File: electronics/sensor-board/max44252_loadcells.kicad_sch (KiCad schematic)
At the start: 21 parts

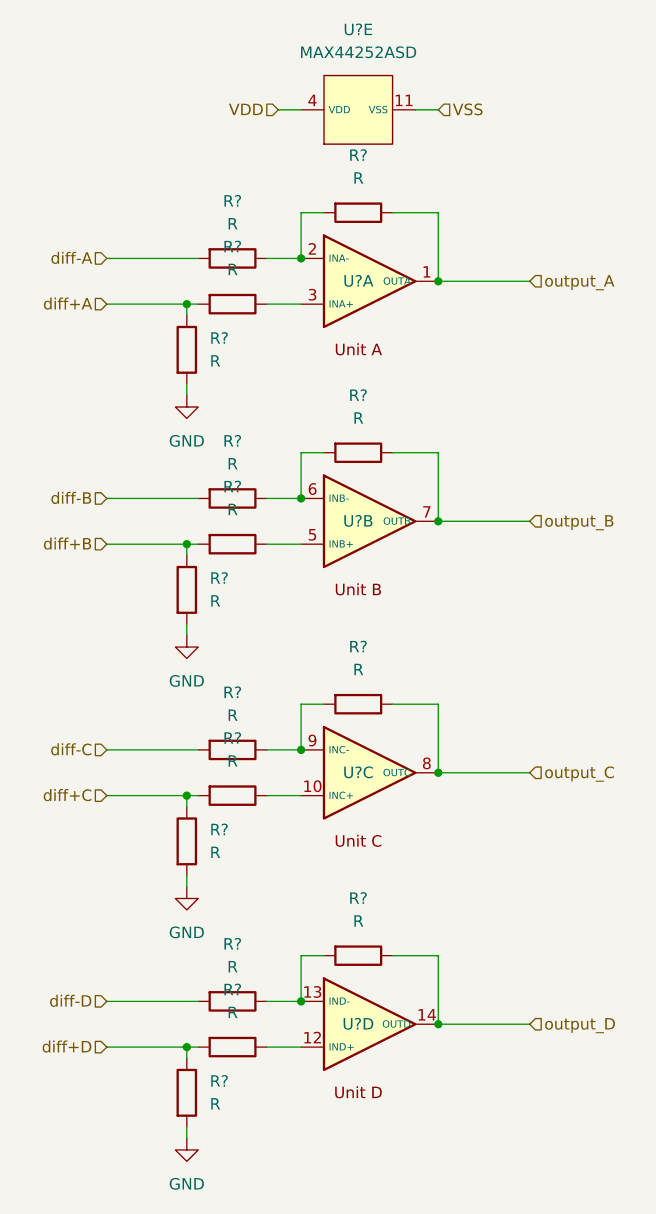
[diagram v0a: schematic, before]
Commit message: work on sensor-board
added MCP960 footprint
finished MCP960 array schematic
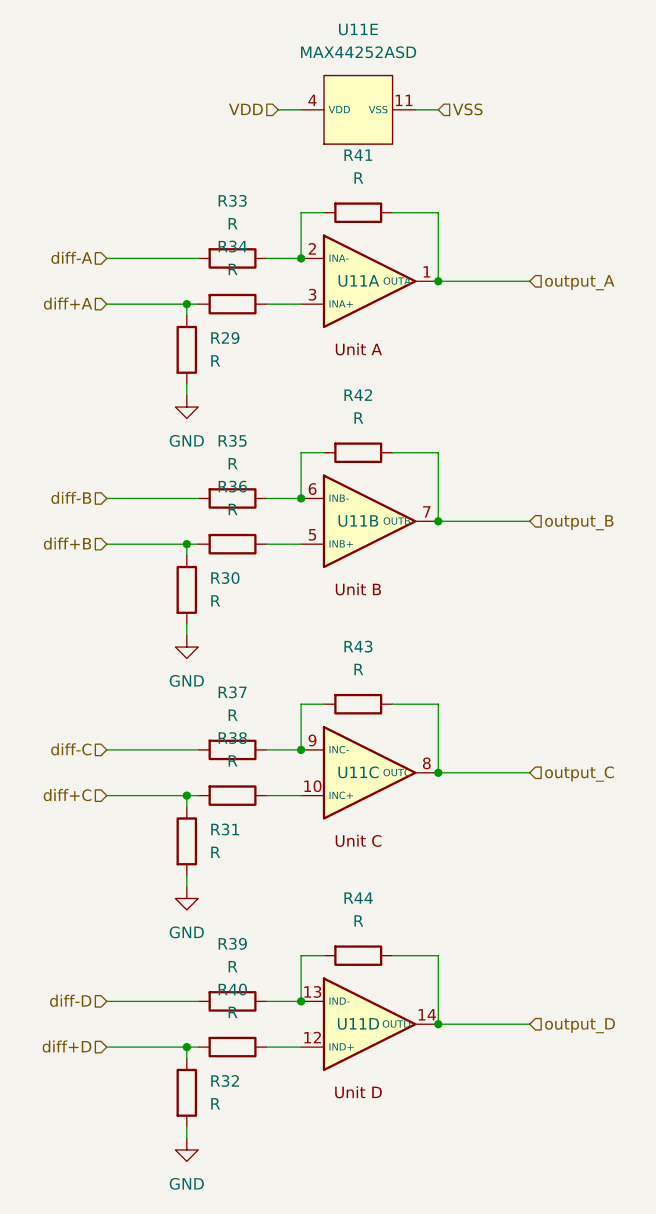
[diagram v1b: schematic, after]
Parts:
- removed R? (x16): R, symbol Device:R
- removed U? (x5): MAX44252ASD, symbol MAX44252ASD_Custom:MAX44252ASD
- added R29, R30, R31, R32, R33, R34, R35, R36, R37, R38, R39, R40, R41, R42, R43, R44: R, Resistor_SMD:R_0603_1608Metric, symbol Device:R
- added U11: MAX44252ASD, MAX44252ASD-:MAX44252ASD&plus_, symbol MAX44252ASD_Custom:MAX44252ASD
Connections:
- net GND: now also R29.2, R30.2, R31.2, R32.2
- net VDD: now also U11.4 (VDD)
- net VSS: now also U11.11 (VSS)
- net diff+A: now also R29.1, R34.2
- net diff+B: now also R30.1, R36.2
- net diff+C: now also R31.1, R38.2
- net diff+D: now also R32.1, R40.2
- net diff-A: now also R33.2
- net diff-B: now also R35.2
- net diff-C: now also R37.2
- net diff-D: now also R39.2
- net output_A: now also R41.1, U11.1 (OUTA)
- net output_B: now also R42.1, U11.7 (OUTB)
- net output_C: now also R43.1, U11.8 (OUTC)
- net output_D: now also R44.1, U11.14 (OUTD)
- new net: R40.1, U11.12 (IND+)
- new net: R34.1, U11.3 (INA+)
- new net: R38.1, U11.10 (INC+)
- new net: R39.1, R44.2, U11.13 (IND-)
- new net: R33.1, R41.2, U11.2 (INA-)
- new net: R37.1, R43.2, U11.9 (INC-)
- new net: R35.1, R42.2, U11.6 (INB-)
- new net: R36.1, U11.5 (INB+)

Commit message: work on sensor-board
finishing sub-circuits
switching mcu to stm32f105
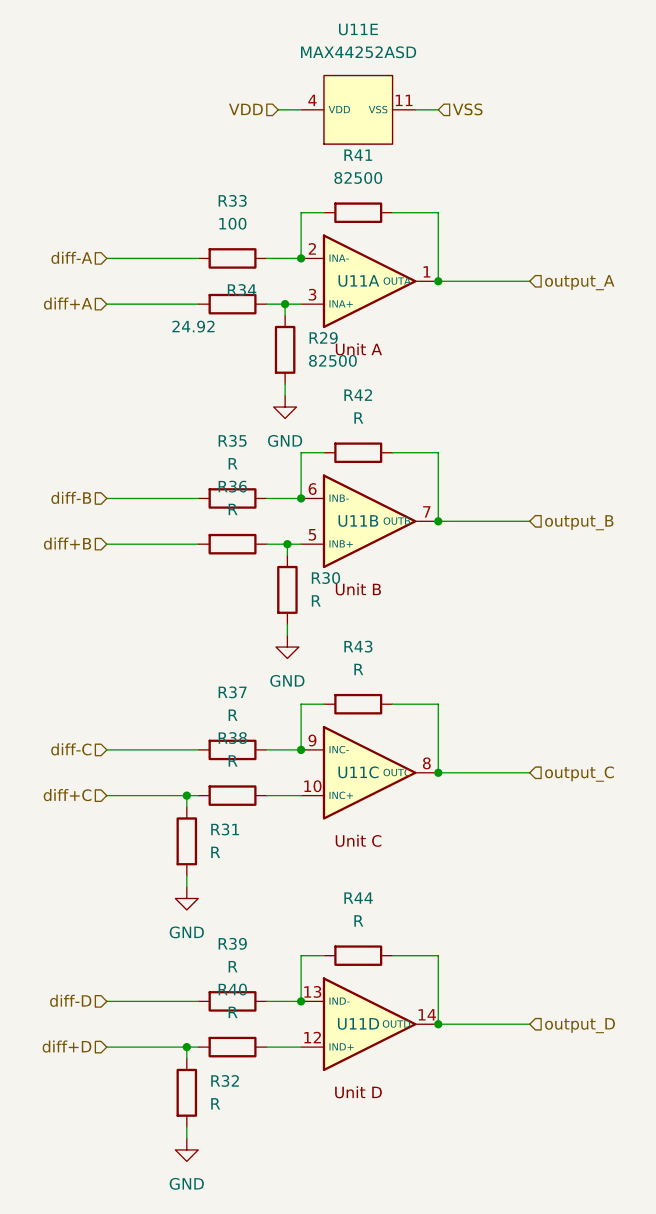
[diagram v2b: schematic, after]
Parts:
- R29, R41: value R -> 82500
- R33: value R -> 100
- R34: value R -> 24.92; note: (none) -> add series res for adjustment
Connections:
- net diff+A: no longer R29.1
- net diff+B: no longer R30.1
- net at R34.1, U11.3 (INA+): now also R29.1
- net at R36.1, U11.5 (INB+): now also R30.1
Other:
- moved on the sheet: R29, R30
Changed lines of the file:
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@@
 (kicad_sch (version 20210621) (generator eeschema)
   (paper "A4")
-  (junction (at 134.62 66.04) (diameter 0) (color 0 0 0 0))
-  (junction (at 134.62 92.71) (diameter 0) (color 0 0 0 0))
   (junction (at 134.62 120.65) (diameter 0) (color 0 0 0 0))
   (junction (at 134.62 148.59) (diameter 0) (color 0 0 0 0))
+  (junction (at 145.542 66.04) (diameter 0) (color 0 0 0 0))
+  (junction (at 145.796 92.71) (diameter 0) (color 0 0 0 0))
   (junction (at 147.32 60.96) (diameter 0) (color 0 0 0 0))
   (junction (at 147.32 87.63) (diameter 0) (color 0 0 0 0))
@@
     (stroke (width 0) (type default) (color 0 0 0 0))
   )
-  (wire (pts (xy 125.73 66.04) (xy 134.62 66.04))
+  (wire (pts (xy 125.73 66.04) (xy 135.89 66.04))
     (stroke (width 0) (type default) (color 0 0 0 0))
   )
@@
     (stroke (width 0) (type default) (color 0 0 0 0))
   )
-  (wire (pts (xy 125.73 92.71) (xy 134.62 92.71))
+  (wire (pts (xy 125.73 92.71) (xy 135.89 92.71))
     (stroke (width 0) (type default) (color 0 0 0 0))
   )
@@
     (stroke (width 0) (type default) (color 0 0 0 0))
   )
-  (wire (pts (xy 134.62 66.04) (xy 134.62 67.31))
-    (stroke (width 0) (type default) (color 0 0 0 0))
-  )
-  (wire (pts (xy 134.62 66.04) (xy 135.89 66.04))
-    (stroke (width 0) (type default) (color 0 0 0 0))
-  )
-  (wire (pts (xy 134.62 74.93) (xy 134.62 76.2))
-    (stroke (width 0) (type default) (color 0 0 0 0))
-  )
-  (wire (pts (xy 134.62 92.71) (xy 134.62 93.98))
-    (stroke (width 0) (type default) (color 0 0 0 0))
-  )
-  (wire (pts (xy 134.62 92.71) (xy 135.89 92.71))
-    (stroke (width 0) (type default) (color 0 0 0 0))
-  )
-  (wire (pts (xy 134.62 101.6) (xy 134.62 102.87))
-    (stroke (width 0) (type default) (color 0 0 0 0))
-  )
   (wire (pts (xy 134.62 120.65) (xy 134.62 121.92))
     (stroke (width 0) (type default) (color 0 0 0 0))
@@
     (stroke (width 0) (type default) (color 0 0 0 0))
   )
-  (wire (pts (xy 143.51 66.04) (xy 147.32 66.04))
+  (wire (pts (xy 143.51 66.04) (xy 145.542 66.04))
     (stroke (width 0) (type default) (color 0 0 0 0))
   )
@@
     (stroke (width 0) (type default) (color 0 0 0 0))
   )
-  (wire (pts (xy 143.51 92.71) (xy 147.32 92.71))
+  (wire (pts (xy 143.51 92.71) (xy 145.796 92.71))
     (stroke (width 0) (type default) (color 0 0 0 0))
   )
@@
   )
   (wire (pts (xy 144.78 44.45) (xy 147.32 44.45))
+    (stroke (width 0) (type default) (color 0 0 0 0))
+  )
+  (wire (pts (xy 145.542 66.04) (xy 145.542 67.31))
+    (stroke (width 0) (type default) (color 0 0 0 0))
+  )
+  (wire (pts (xy 145.542 66.04) (xy 147.32 66.04))
+    (stroke (width 0) (type default) (color 0 0 0 0))
+  )
+  (wire (pts (xy 145.542 74.93) (xy 145.542 76.2))
+    (stroke (width 0) (type default) (color 0 0 0 0))
+  )
+  (wire (pts (xy 145.796 92.71) (xy 145.796 93.98))
+    (stroke (width 0) (type default) (color 0 0 0 0))
+  )
+  (wire (pts (xy 145.796 92.71) (xy 147.32 92.71))
+    (stroke (width 0) (type default) (color 0 0 0 0))
+  )
+  (wire (pts (xy 145.796 101.6) (xy 145.796 102.87))
     (stroke (width 0) (type default) (color 0 0 0 0))
   )
@@
     (effects (font (size 1.27 1.27)) (justify left))
   )
-  (symbol (lib_id "power:GND") (at 134.62 76.2 0) (unit 1)
-    (in_bom yes) (on_board yes) (fields_autoplaced)
-    (property "Reference" "#PWR0175" (id 0) (at 134.62 82.55 0)
-      (effects (font (size 1.27 1.27)) hide)
-    )
-    (property "Value" "GND" (id 1) (at 134.62 81.28 0))
-    (property "Footprint" "" (id 2) (at 134.62 76.2 0)
-      (effects (font (size 1.27 1.27)) hide)
-    )
-    (property "Datasheet" "" (id 3) (at 134.62 76.2 0)
-      (effects (font (size 1.27 1.27)) hide)
-    )
-    (pin "1")
-  )
-  (symbol (lib_id "power:GND") (at 134.62 102.87 0) (unit 1)
-    (in_bom yes) (on_board yes) (fields_autoplaced)
-    (property "Reference" "#PWR0176" (id 0) (at 134.62 109.22 0)
-      (effects (font (size 1.27 1.27)) hide)
-    )
-    (property "Value" "GND" (id 1) (at 134.62 107.95 0))
-    (property "Footprint" "" (id 2) (at 134.62 102.87 0)
-      (effects (font (size 1.27 1.27)) hide)
-    )
-    (property "Datasheet" "" (id 3) (at 134.62 102.87 0)
-      (effects (font (size 1.27 1.27)) hide)
-    )
-    (pin "1")
-  )
   (symbol (lib_id "power:GND") (at 134.62 130.81 0) (unit 1)
     (in_bom yes) (on_board yes) (fields_autoplaced)
@@
     (pin "1")
   )
-  (symbol (lib_id "Device:R") (at 134.62 71.12 0) (unit 1)
-    (in_bom yes) (on_board yes) (fields_autoplaced)
-    (property "Reference" "R29" (id 0) (at 137.16 69.8499 0)
-      (effects (font (size 1.27 1.27)) (justify left))
-    )
-    (property "Value" "R" (id 1) (at 137.16 72.3899 0)
-      (effects (font (size 1.27 1.27)) (justify left))
-    )
-    (property "Footprint" "Resistor_SMD:R_0603_1608Metric" (id 2) (at 132.842 71.12 90)
-      (effects (font (size 1.27 1.27)) hide)
-    )
-    (property "Datasheet" "~" (id 3) (at 134.62 71.12 0)
-      (effects (font (size 1.27 1.27)) hide)
-    )
-    (pin "1")
-    (pin "2")
-  )
-  (symbol (lib_id "Device:R") (at 134.62 97.79 0) (unit 1)
-    (in_bom yes) (on_board yes) (fields_autoplaced)
-    (property "Reference" "R30" (id 0) (at 137.16 96.5199 0)
-      (effects (font (size 1.27 1.27)) (justify left))
-    )
-    (property "Value" "R" (id 1) (at 137.16 99.0599 0)
-      (effects (font (size 1.27 1.27)) (justify left))
-    )
-    (property "Footprint" "Resistor_SMD:R_0603_1608Metric" (id 2) (at 132.842 97.79 90)
-      (effects (font (size 1.27 1.27)) hide)
-    )
-    (property "Datasheet" "~" (id 3) (at 134.62 97.79 0)
-      (effects (font (size 1.27 1.27)) hide)
-    )
-    (pin "1")
-    (pin "2")
+  (symbol (lib_id "power:GND") (at 145.542 76.2 0) (unit 1)
+    (in_bom yes) (on_board yes) (fields_autoplaced)
+    (property "Reference" "#PWR0175" (id 0) (at 145.542 82.55 0)
+      (effects (font (size 1.27 1.27)) hide)
+    )
+    (property "Value" "GND" (id 1) (at 145.542 81.28 0))
+    (property "Footprint" "" (id 2) (at 145.542 76.2 0)
+      (effects (font (size 1.27 1.27)) hide)
+    )
+    (property "Datasheet" "" (id 3) (at 145.542 76.2 0)
+      (effects (font (size 1.27 1.27)) hide)
+    )
+    (pin "1")
+  )
+  (symbol (lib_id "power:GND") (at 145.796 102.87 0) (unit 1)
+    (in_bom yes) (on_board yes) (fields_autoplaced)
+    (property "Reference" "#PWR0176" (id 0) (at 145.796 109.22 0)
+      (effects (font (size 1.27 1.27)) hide)
+    )
+    (property "Value" "GND" (id 1) (at 145.796 107.95 0))
+    (property "Footprint" "" (id 2) (at 145.796 102.87 0)
+      (effects (font (size 1.27 1.27)) hide)
+    )
+    (property "Datasheet" "" (id 3) (at 145.796 102.87 0)
+      (effects (font (size 1.27 1.27)) hide)
+    )
+    (pin "1")
   )
   (symbol (lib_id "Device:R") (at 134.62 125.73 0) (unit 1)
@@
     (in_bom yes) (on_board yes) (fields_autoplaced)
     (property "Reference" "R33" (id 0) (at 139.7 54.61 90))
-    (property "Value" "R" (id 1) (at 139.7 57.15 90))
+    (property "Value" "100" (id 1) (at 139.7 57.15 90))
     (property "Footprint" "Resistor_SMD:R_0603_1608Metric" (id 2) (at 139.7 59.182 90)
       (effects (font (size 1.27 1.27)) hide)
@@
   )
   (symbol (lib_id "Device:R") (at 139.7 66.04 270) (unit 1)
-    (in_bom yes) (on_board yes) (fields_autoplaced)
-    (property "Reference" "R34" (id 0) (at 139.7 59.69 90))
-    (property "Value" "R" (id 1) (at 139.7 62.23 90))
+    (in_bom yes) (on_board yes)
+    (property "Reference" "R34" (id 0) (at 140.716 64.516 90))
+    (property "Value" "24.92" (id 1) (at 135.382 68.58 90))
     (property "Footprint" "Resistor_SMD:R_0603_1608Metric" (id 2) (at 139.7 64.262 90)
       (effects (font (size 1.27 1.27)) hide)
     )
     (property "Datasheet" "~" (id 3) (at 139.7 66.04 0)
+      (effects (font (size 1.27 1.27)) hide)
+    )
+    (property "note:" "add series res for adjustment" (id 4) (at 139.7 66.04 90)
       (effects (font (size 1.27 1.27)) hide)
     )
@@
     (pin "2")
   )
+  (symbol (lib_id "Device:R") (at 145.542 71.12 0) (unit 1)
+    (in_bom yes) (on_board yes) (fields_autoplaced)
+    (property "Reference" "R29" (id 0) (at 148.082 69.8499 0)
+      (effects (font (size 1.27 1.27)) (justify left))
+    )
+    (property "Value" "82500" (id 1) (at 148.082 72.3899 0)
+      (effects (font (size 1.27 1.27)) (justify left))
+    )
+    (property "Footprint" "Resistor_SMD:R_0603_1608Metric" (id 2) (at 143.764 71.12 90)
+      (effects (font (size 1.27 1.27)) hide)
+    )
+    (property "Datasheet" "~" (id 3) (at 145.542 71.12 0)
+      (effects (font (size 1.27 1.27)) hide)
+    )
+    (pin "1")
+    (pin "2")
+  )
+  (symbol (lib_id "Device:R") (at 145.796 97.79 0) (unit 1)
+    (in_bom yes) (on_board yes) (fields_autoplaced)
+    (property "Reference" "R30" (id 0) (at 148.336 96.5199 0)
+      (effects (font (size 1.27 1.27)) (justify left))
+    )
+    (property "Value" "R" (id 1) (at 148.336 99.0599 0)
+      (effects (font (size 1.27 1.27)) (justify left))
+    )
+    (property "Footprint" "Resistor_SMD:R_0603_1608Metric" (id 2) (at 144.018 97.79 90)
+      (effects (font (size 1.27 1.27)) hide)
+    )
+    (property "Datasheet" "~" (id 3) (at 145.796 97.79 0)
+      (effects (font (size 1.27 1.27)) hide)
+    )
+    (pin "1")
+    (pin "2")
+  )
   (symbol (lib_id "Device:R") (at 153.67 55.88 270) (unit 1)
     (in_bom yes) (on_board yes) (fields_autoplaced)
     (property "Reference" "R41" (id 0) (at 153.67 49.53 90))
-    (property "Value" "R" (id 1) (at 153.67 52.07 90))
+    (property "Value" "82500" (id 1) (at 153.67 52.07 90))
     (property "Footprint" "Resistor_SMD:R_0603_1608Metric" (id 2) (at 153.67 54.102 90)
       (effects (font (size 1.27 1.27)) hide)

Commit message: Finalized sensor-board schematic
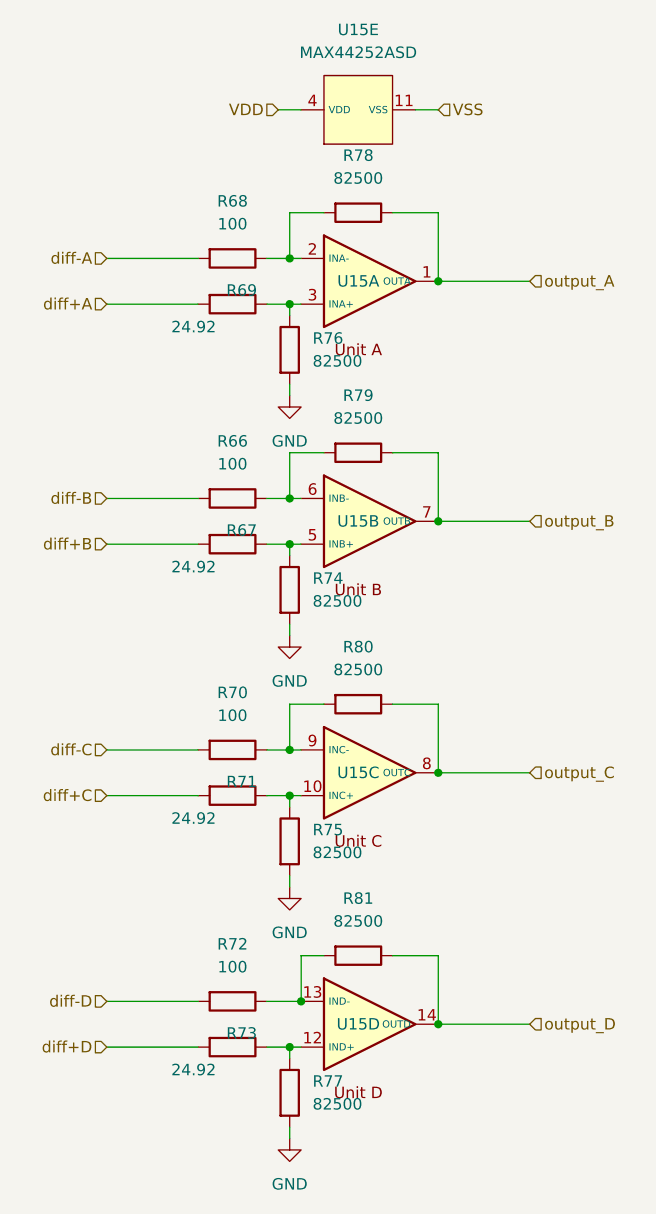
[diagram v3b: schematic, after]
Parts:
- removed R30, R31, R32, R35, R36, R37, R38, R39, R40, R42, R43, R44: R, Resistor_SMD:R_0603_1608Metric, symbol Device:R
- added R66, R70, R72: 100, Resistor_SMD:R_0603_1608Metric, symbol Device:R
- added R67, R71, R73: 24.92, Resistor_SMD:R_0603_1608Metric, symbol Device:R
- added R74, R75, R77, R79, R80, R81: 82500, Resistor_SMD:R_0603_1608Metric, symbol Device:R
- renumbered R33 to R68, R34 to R69, R29 to R76, R41 to R78, U11 to U15
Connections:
- net GND: now also R74.2, R75.2, R77.2
- net diff+B: now also R67.2
- net diff+C: now also R71.2
- net diff+D: now also R73.2
- net diff-B: now also R66.2
- net diff-C: now also R70.2
- net diff-D: now also R72.2
- net output_B: now also R79.1
- net output_C: now also R80.1
- net output_D: now also R81.1
- net at U15.12 (IND+): now also R73.1, R77.1
- net at U15.10 (INC+): now also R71.1, R75.1
- net at U15.13 (IND-): now also R72.1, R81.2
- net at U15.9 (INC-): now also R70.1, R80.2
- net at U15.6 (INB-): now also R66.1, R79.2
- net at U15.5 (INB+): now also R67.1, R74.1
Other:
- moved on the sheet: R76
